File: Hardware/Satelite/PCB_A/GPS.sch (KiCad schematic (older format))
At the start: 8 parts, among them U1 A2235-H

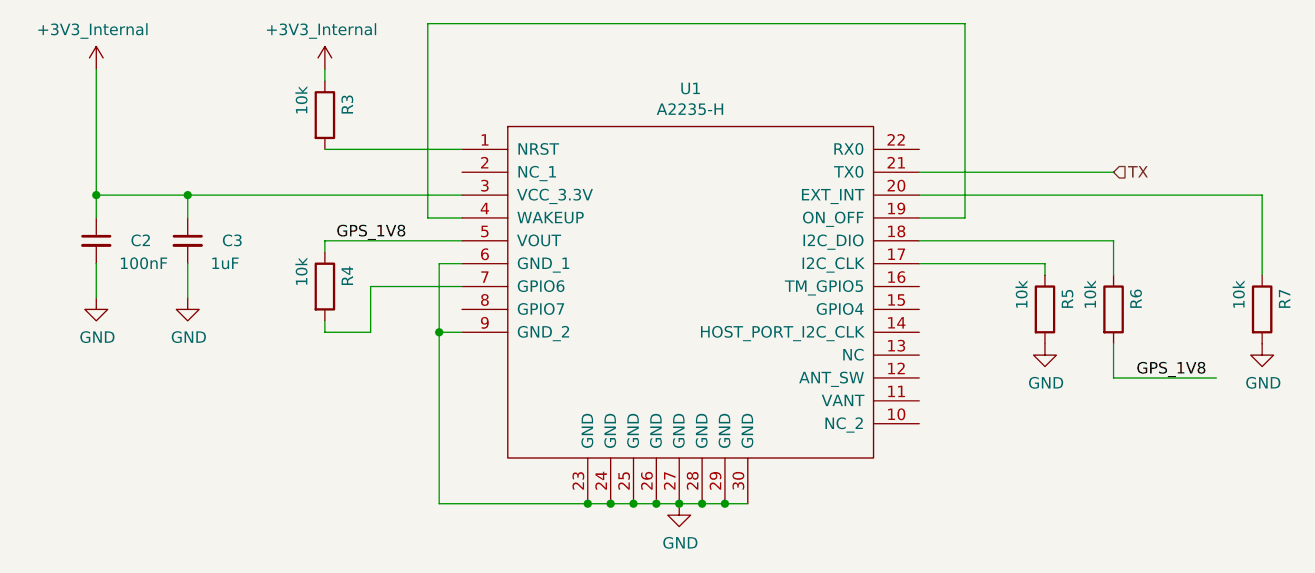
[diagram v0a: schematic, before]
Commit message: Numeros de parte para PCB_A. Se movió también el switch de encendido más afuera para fácil acceso.
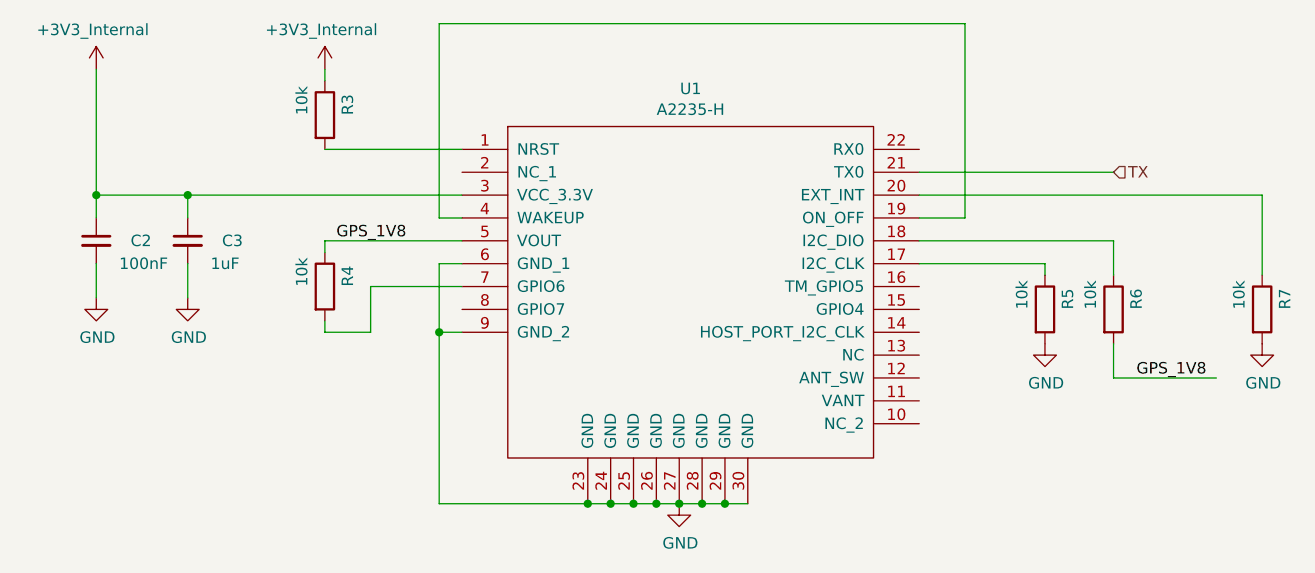
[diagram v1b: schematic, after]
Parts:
- C2: Manufacturer Part Number (none) -> GCM155R71C104KA55D
- C3: Manufacturer Part Number (none) -> GRM155R61E105KA12D
- R3, R4, R5, R6, R7: Manufacturer Part Number (none) -> RC0603JR-0710KL
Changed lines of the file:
@@
 $EndComp
 Wire Wire Line
-	4700 3100 4550 3100
-Wire Wire Line
-	4550 3100 4550 2250
-Wire Wire Line
-	4550 2250 6900 2250
+	4700 3100 4600 3100
+Wire Wire Line
+	4600 3100 4600 2250
+Wire Wire Line
+	4600 2250 6900 2250
 Wire Wire Line
 	6900 2250 6900 3100
 Wire Wire Line
 	6900 3100 6700 3100
-$Comp
-L Device:R R?
-U 1 1 5BAD7E11
-P 4100 3400
-AR Path="/5BA17F9C/5BAD7E11" Ref="R?"  Part="1"
-AR Path="/5BA1A7F9/5BAD7E11" Ref="R4"  Part="1"
-F 0 "R4" V 4200 3400 50  0000 L CNN
-F 1 "10k" V 4000 3400 50  0000 L CNN
-F 2 "Resistor_SMD:R_0603_1608Metric_Pad1.05x0.95mm_HandSolder" V 4030 3400 50  0001 C CNN
-F 3 "~" H 4100 3400 50  0001 C CNN
-	1    4100 3400
-	1    0    0    -1
-$EndComp
 Wire Wire Line
 	4700 3200 4100 3200
@@
 F 2 "Resistor_SMD:R_0603_1608Metric_Pad1.05x0.95mm_HandSolder" V 4030 2650 50  0001 C CNN
 F 3 "~" H 4100 2650 50  0001 C CNN
+F 4 "RC0603JR-0710KL" V 4100 2650 50  0001 C CNN "Manufacturer Part Number"
 	1    4100 2650
 	1    0    0    -1
@@
 Wire Wire Line
 	4600 3600 4600 4350
-$Comp
-L Device:R R?
-U 1 1 5BADA56C
-P 7250 3500
-AR Path="/5BA17F9C/5BADA56C" Ref="R?"  Part="1"
-AR Path="/5BA1A7F9/5BADA56C" Ref="R5"  Part="1"
-F 0 "R5" V 7350 3500 50  0000 L CNN
-F 1 "10k" V 7150 3500 50  0000 L CNN
-F 2 "Resistor_SMD:R_0603_1608Metric_Pad1.05x0.95mm_HandSolder" V 7180 3500 50  0001 C CNN
-F 3 "~" H 7250 3500 50  0001 C CNN
-	1    7250 3500
-	1    0    0    -1
-$EndComp
-$Comp
-L Device:R R?
-U 1 1 5BADA5CC
-P 7550 3500
-AR Path="/5BA17F9C/5BADA5CC" Ref="R?"  Part="1"
-AR Path="/5BA1A7F9/5BADA5CC" Ref="R6"  Part="1"
-F 0 "R6" V 7650 3500 50  0000 L CNN
-F 1 "10k" V 7450 3500 50  0000 L CNN
-F 2 "Resistor_SMD:R_0603_1608Metric_Pad1.05x0.95mm_HandSolder" V 7480 3500 50  0001 C CNN
-F 3 "~" H 7550 3500 50  0001 C CNN
-	1    7550 3500
-	1    0    0    -1
-$EndComp
 Wire Wire Line
 	6700 3300 7250 3300
@@
 F 2 "Capacitor_SMD:C_0603_1608Metric_Pad1.05x0.95mm_HandSolder" H 3500 3200 50  0001 C CNN
 F 3 "~" H 3500 3200 50  0001 C CNN
+F 4 "GRM155R61E105KA12D" H 3500 3200 50  0001 C CNN "Manufacturer Part Number"
 	1    3500 3200
 	1    0    0    -1
@@
 F 2 "Capacitor_SMD:C_0603_1608Metric_Pad1.05x0.95mm_HandSolder" H 3100 3200 50  0001 C CNN
 F 3 "~" H 3100 3200 50  0001 C CNN
+F 4 "GCM155R71C104KA55D" H 3100 3200 50  0001 C CNN "Manufacturer Part Number"
 	1    3100 3200
 	1    0    0    -1
@@
 Connection ~ 3500 3000
 Connection ~ 3100 3000
-$Comp
-L Device:R R?
-U 1 1 5BAE0532
-P 8200 3500
-AR Path="/5BA17F9C/5BAE0532" Ref="R?"  Part="1"
-AR Path="/5BA1A7F9/5BAE0532" Ref="R7"  Part="1"
-F 0 "R7" V 8300 3500 50  0000 L CNN
-F 1 "10k" V 8100 3500 50  0000 L CNN
-F 2 "Resistor_SMD:R_0603_1608Metric_Pad1.05x0.95mm_HandSolder" V 8130 3500 50  0001 C CNN
-F 3 "~" H 8200 3500 50  0001 C CNN
-	1    8200 3500
-	1    0    0    -1
-$EndComp
 Wire Wire Line
 	8200 3000 6700 3000
@@
 Wire Wire Line
 	3100 2450 3100 3000
+$Comp
+L Device:R R?
+U 1 1 5C2659D3
+P 4100 3400
+AR Path="/5BA17F9C/5C2659D3" Ref="R?"  Part="1"
+AR Path="/5BA1A7F9/5C2659D3" Ref="R4"  Part="1"
+F 0 "R4" V 4200 3400 50  0000 L CNN
+F 1 "10k" V 4000 3400 50  0000 L CNN
+F 2 "Resistor_SMD:R_0603_1608Metric_Pad1.05x0.95mm_HandSolder" V 4030 3400 50  0001 C CNN
+F 3 "~" H 4100 3400 50  0001 C CNN
+F 4 "RC0603JR-0710KL" V 4100 3400 50  0001 C CNN "Manufacturer Part Number"
+	1    4100 3400
+	1    0    0    -1
+$EndComp
+$Comp
+L Device:R R?
+U 1 1 5C265A87
+P 7250 3500
+AR Path="/5BA17F9C/5C265A87" Ref="R?"  Part="1"
+AR Path="/5BA1A7F9/5C265A87" Ref="R5"  Part="1"
+F 0 "R5" V 7350 3500 50  0000 L CNN
+F 1 "10k" V 7150 3500 50  0000 L CNN
+F 2 "Resistor_SMD:R_0603_1608Metric_Pad1.05x0.95mm_HandSolder" V 7180 3500 50  0001 C CNN
+F 3 "~" H 7250 3500 50  0001 C CNN
+F 4 "RC0603JR-0710KL" V 7250 3500 50  0001 C CNN "Manufacturer Part Number"
+	1    7250 3500
+	1    0    0    -1
+$EndComp
+$Comp
+L Device:R R?
+U 1 1 5C265B51
+P 7550 3500
+AR Path="/5BA17F9C/5C265B51" Ref="R?"  Part="1"
+AR Path="/5BA1A7F9/5C265B51" Ref="R6"  Part="1"
+F 0 "R6" V 7650 3500 50  0000 L CNN
+F 1 "10k" V 7450 3500 50  0000 L CNN
+F 2 "Resistor_SMD:R_0603_1608Metric_Pad1.05x0.95mm_HandSolder" V 7480 3500 50  0001 C CNN
+F 3 "~" H 7550 3500 50  0001 C CNN
+F 4 "RC0603JR-0710KL" V 7550 3500 50  0001 C CNN "Manufacturer Part Number"
+	1    7550 3500
+	1    0    0    -1
+$EndComp
+$Comp
+L Device:R R?
+U 1 1 5C265C3F
+P 8200 3500
+AR Path="/5BA17F9C/5C265C3F" Ref="R?"  Part="1"
+AR Path="/5BA1A7F9/5C265C3F" Ref="R7"  Part="1"
+F 0 "R7" V 8300 3500 50  0000 L CNN
+F 1 "10k" V 8100 3500 50  0000 L CNN
+F 2 "Resistor_SMD:R_0603_1608Metric_Pad1.05x0.95mm_HandSolder" V 8130 3500 50  0001 C CNN
+F 3 "~" H 8200 3500 50  0001 C CNN
+F 4 "RC0603JR-0710KL" V 8200 3500 50  0001 C CNN "Manufacturer Part Number"
+	1    8200 3500
+	1    0    0    -1
+$EndComp
 $EndSCHEMATC

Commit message: BOM para PCB_A y corrección de algunos numeros de parte
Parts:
- C3: Manufacturer Part Number GRM155R61E105KA12D -> LMK107B7105MA-T
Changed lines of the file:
@@
 F 2 "Capacitor_SMD:C_0603_1608Metric_Pad1.05x0.95mm_HandSolder" H 3500 3200 50  0001 C CNN
 F 3 "~" H 3500 3200 50  0001 C CNN
-F 4 "GRM155R61E105KA12D" H 3500 3200 50  0001 C CNN "Manufacturer Part Number"
+F 4 "LMK107B7105MA-T" H 3500 3200 50  0001 C CNN "Manufacturer Part Number"
 	1    3500 3200
 	1    0    0    -1

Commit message: Corrección de numero de partes en PCB_A
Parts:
- C2: footprint Capacitor_SMD:C_0603_1608Metric_Pad1.05x0.95mm_HandSolder -> Capacitor_SMD:C_0402_1005Metric
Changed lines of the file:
@@
 F 0 "C2" H 3250 3200 50  0000 L CNN
 F 1 "100nF" H 3200 3100 50  0000 L CNN
-F 2 "Capacitor_SMD:C_0603_1608Metric_Pad1.05x0.95mm_HandSolder" H 3100 3200 50  0001 C CNN
+F 2 "Capacitor_SMD:C_0402_1005Metric" H 3100 3200 50  0001 C CNN
 F 3 "~" H 3100 3200 50  0001 C CNN
 F 4 "GCM155R71C104KA55D" H 3100 3200 50  0001 C CNN "Manufacturer Part Number"
